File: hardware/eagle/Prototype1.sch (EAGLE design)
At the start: 27 parts, among them U1 ARDUINO_SHIELDLABEL

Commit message: Wege bahnen WIP
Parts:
- removed LED1: (no value), led:LEDKA-3528ASYC
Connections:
- net N$11: now also RED5.C, U$2.LED2; no longer BLUE5.C, U$2.LED15
- net N$12: now also U$2.LED3; no longer U$2.LED14
- net N$13: now also BLUE5.C, U$2.LED4; no longer RED5.C, U$2.LED13
- net N$14: now also U$2.LED5; no longer U$2.LED12
- net N$15: now also U$2.LED7; no longer U$2.LED10
- net N$16: now also U$2.LED6; no longer U$2.LED11
- net N$17: now also U$2.LED8; no longer U$2.LED9
- net N$18: now also U$2.LED9; no longer U$2.LED8
- net N$19: now also U$2.LED10; no longer U$2.LED7
- net N$20: now also U$2.LED11; no longer U$2.LED6
- net N$21: now also U$2.LED12; no longer U$2.LED5
- net N$22: now also U$2.LED13; no longer U$2.LED4
- net N$23: now also U$2.LED14; no longer U$2.LED3
- net N$24: now also U$2.LED15; no longer U$2.LED2
- net N$25: now also U$2.LED16; no longer U$2.LED1

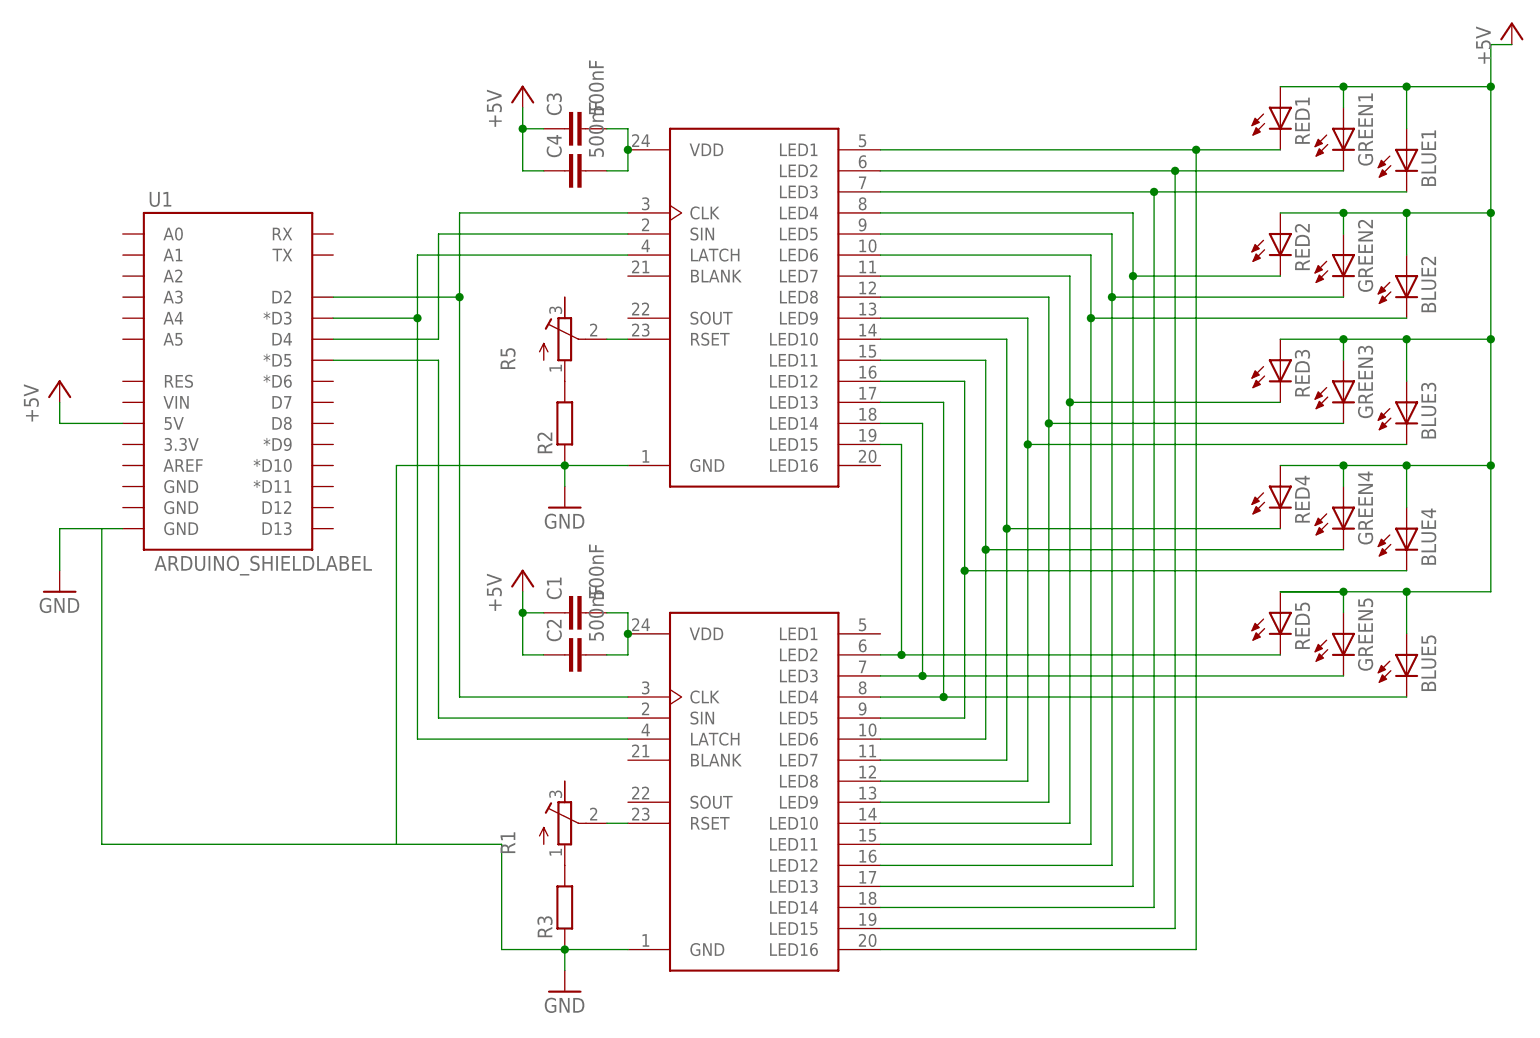
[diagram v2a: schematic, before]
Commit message: Prototyp 1 verkabelt
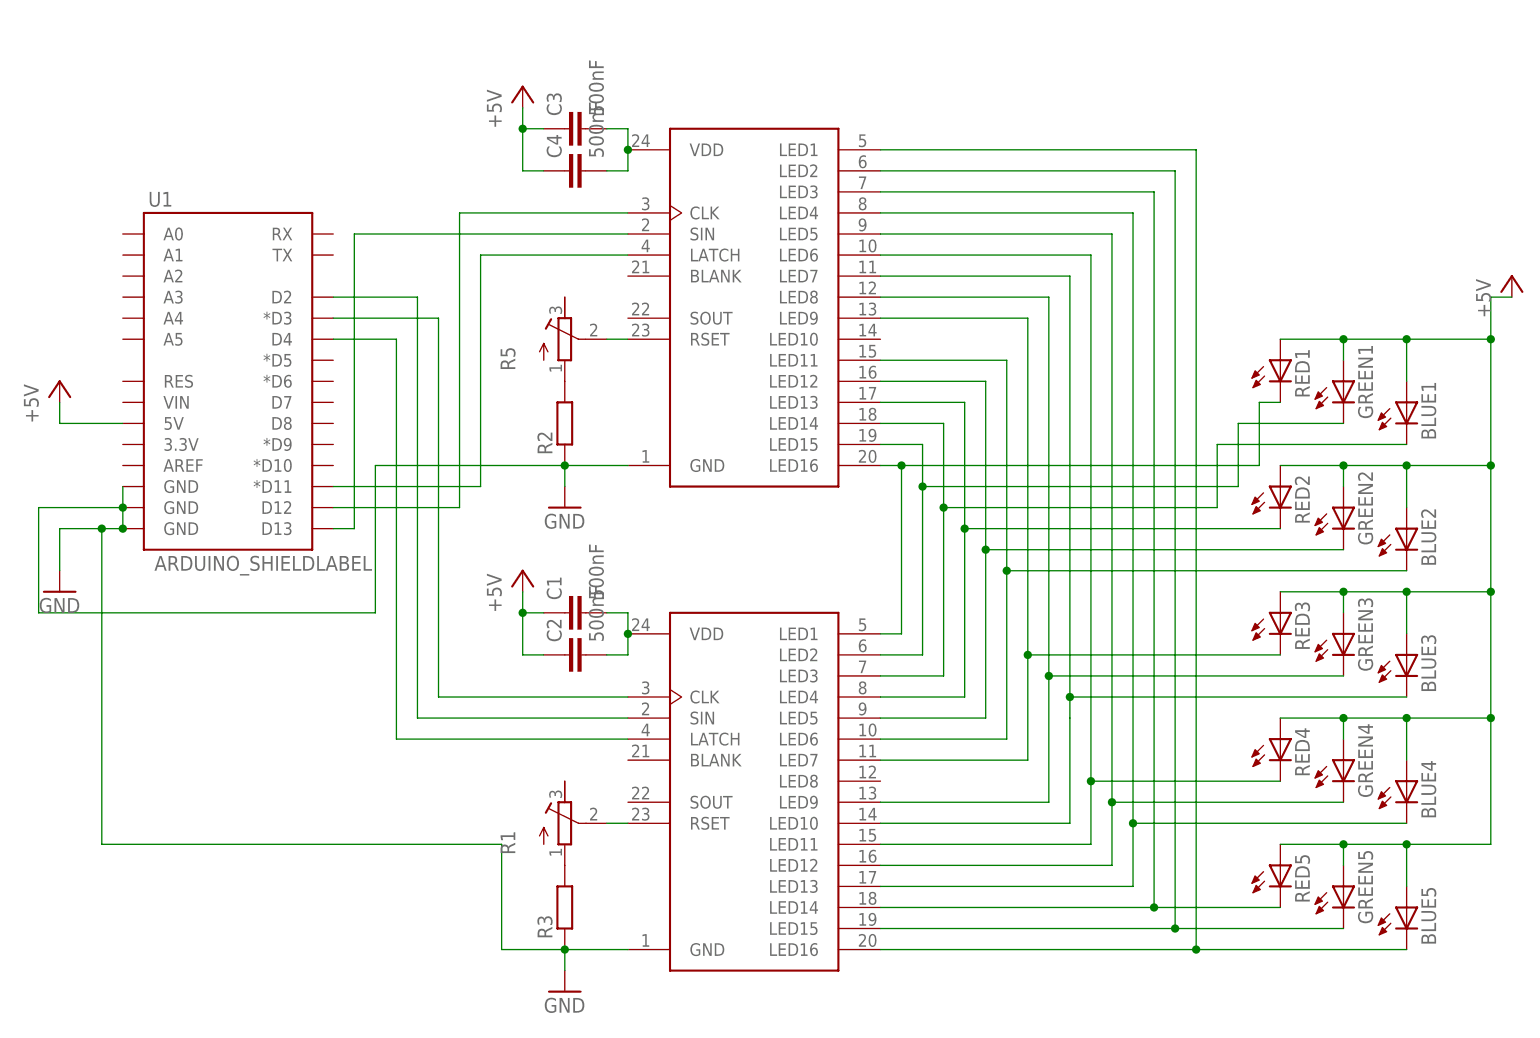
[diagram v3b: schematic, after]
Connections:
- new net N$31: U$3.LATCH, U1.*D11
- new net N$39: BLUE5.C, U$2.LED16, U$3.LED1
- net GND: now also U1.GND@1, U1.GND@2
- net N$10: now also U1.D2; no longer U1.*D5
- net N$11: now also GREEN2.C, U$2.LED5, U$3.LED12; no longer RED5.C, U$2.LED2, U$3.LED15
- net N$12: now also RED2.C, U$2.LED4, U$3.LED13; no longer GREEN5.C, U$2.LED3, U$3.LED14
- net N$13: now also BLUE1.C, U$2.LED3, U$3.LED14; no longer BLUE5.C, U$2.LED4, U$3.LED13
- net N$14: now also GREEN1.C, U$2.LED2, U$3.LED15; no longer BLUE4.C, U$2.LED5, U$3.LED12
- net N$15: now also BLUE2.C, U$2.LED6, U$3.LED11; no longer RED4.C, U$2.LED7, U$3.LED10
- net N$16: now also RED1.C, U$2.LED1, U$3.LED16; no longer GREEN4.C, U$2.LED6, U$3.LED11
- net N$17: now also RED3.C, U$2.LED7; no longer BLUE3.C, U$2.LED8
- net N$19: now also BLUE3.C; no longer RED3.C
- net N$20: now also RED4.C; no longer BLUE2.C
- net N$21: now also GREEN4.C; no longer GREEN2.C
- net N$22: now also BLUE4.C; no longer RED2.C
- net N$23: now also RED5.C; no longer BLUE1.C
- net N$24: now also GREEN5.C; no longer GREEN1.C
- net N$25: now also U$3.CLK, U1.D12; no longer RED1.C, U$2.LED16, U$3.LED1
- net N$7: now also U1.*D3; no longer U$3.CLK, U1.D2
- net N$8: now also U1.D4; no longer U$3.LATCH, U1.*D3
- net N$9: now also U1.D13; no longer U1.D4
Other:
- moved on the sheet: BLUE1, BLUE2, BLUE3, BLUE4, BLUE5, GREEN1, GREEN2, GREEN3, GREEN4, GREEN5, RED1, RED2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

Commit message: finished Prototype1, created gerber
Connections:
- removed net N$1: C1.2, C2.2, U$2.VDD
- removed net N$6: C3.2, C4.2, U$3.VDD
- net +5V: now also C1.2, C2.2, C3.2, C4.2, U$2.VDD, U$3.VDD; no longer C1.1, C2.1, C3.1, C4.1
- net GND: now also C1.1, C2.1, C3.1, C4.1, U$2.BLANK, U$3.BLANK
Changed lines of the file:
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@@
 <part name="GREEN5" library="led" deviceset="LED" device="KA-3528ASYC"/>
 <part name="P+4" library="supply1" deviceset="+5V" device=""/>
+<part name="GND4" library="supply1" deviceset="GND" device=""/>
+<part name="GND5" library="supply1" deviceset="GND" device=""/>
 </parts>
 <sheets>
@@
 <instance part="C2" gate="G$1" x="73.66" y="10.16" rot="R90"/>
 <instance part="U$2" gate="G$1" x="93.98" y="-5.08"/>
-<instance part="P+2" gate="1" x="66.04" y="20.32"/>
+<instance part="P+2" gate="1" x="78.74" y="17.78"/>
 <instance part="R3" gate="G$1" x="71.12" y="-20.32" rot="R90"/>
 <instance part="R1" gate="G$1" x="71.12" y="-10.16"/>
@@
 <instance part="C4" gate="G$1" x="73.66" y="68.58" rot="R90"/>
 <instance part="U$3" gate="G$1" x="93.98" y="53.34"/>
-<instance part="P+3" gate="1" x="66.04" y="78.74"/>
+<instance part="P+3" gate="1" x="78.74" y="76.2"/>
 <instance part="R2" gate="G$1" x="71.12" y="38.1" rot="R90"/>
 <instance part="R5" gate="G$1" x="71.12" y="48.26"/>
@@
 <instance part="GREEN5" gate="G$1" x="165.1" y="-17.78"/>
 <instance part="P+4" gate="1" x="185.42" y="55.88"/>
+<instance part="GND4" gate="1" x="66.04" y="66.04"/>
+<instance part="GND5" gate="1" x="66.04" y="7.62"/>
 </instances>
 <busses>
@@
 <pinref part="U$3" gate="G$1" pin="GND"/>
 <wire x1="78.74" y1="33.02" x2="71.12" y2="33.02" width="0.1524" layer="91"/>
-<wire x1="71.12" y1="33.02" x2="71.12" y2="30.48" width="0.1524" layer="91"/>
 <junction x="71.12" y="33.02"/>
-<wire x1="48.26" y1="33.02" x2="71.12" y2="33.02" width="0.1524" layer="91"/>
+<wire x1="48.26" y1="33.02" x2="63.5" y2="33.02" width="0.1524" layer="91"/>
 <wire x1="48.26" y1="33.02" x2="48.26" y2="15.24" width="0.1524" layer="91"/>
 <wire x1="48.26" y1="15.24" x2="7.62" y2="15.24" width="0.1524" layer="91"/>
@@
 <junction x="17.78" y="25.4"/>
 <junction x="15.24" y="25.4"/>
+<pinref part="U$3" gate="G$1" pin="BLANK"/>
+<wire x1="78.74" y1="55.88" x2="63.5" y2="55.88" width="0.1524" layer="91"/>
+<wire x1="63.5" y1="55.88" x2="63.5" y2="33.02" width="0.1524" layer="91"/>
+<wire x1="63.5" y1="33.02" x2="71.12" y2="33.02" width="0.1524" layer="91"/>
+<wire x1="71.12" y1="33.02" x2="71.12" y2="30.48" width="0.1524" layer="91"/>
+<junction x="63.5" y="33.02"/>
+<pinref part="U$2" gate="G$1" pin="BLANK"/>
+<wire x1="78.74" y1="-2.54" x2="63.5" y2="-2.54" width="0.1524" layer="91"/>
+<wire x1="63.5" y1="-2.54" x2="63.5" y2="-12.7" width="0.1524" layer="91"/>
+<junction x="63.5" y="-12.7"/>
+</segment>
+<segment>
+<pinref part="C3" gate="G$1" pin="1"/>
+<wire x1="68.58" y1="73.66" x2="66.04" y2="73.66" width="0.1524" layer="91"/>
+<pinref part="C4" gate="G$1" pin="1"/>
+<wire x1="68.58" y1="68.58" x2="66.04" y2="68.58" width="0.1524" layer="91"/>
+<wire x1="66.04" y1="68.58" x2="66.04" y2="73.66" width="0.1524" layer="91"/>
+<pinref part="GND4" gate="1" pin="GND"/>
+<junction x="66.04" y="68.58"/>
+</segment>
+<segment>
+<pinref part="C1" gate="G$1" pin="1"/>
+<wire x1="68.58" y1="15.24" x2="66.04" y2="15.24" width="0.1524" layer="91"/>
+<pinref part="C2" gate="G$1" pin="1"/>
+<wire x1="68.58" y1="10.16" x2="66.04" y2="10.16" width="0.1524" layer="91"/>
+<wire x1="66.04" y1="10.16" x2="66.04" y2="15.24" width="0.1524" layer="91"/>
+<pinref part="GND5" gate="1" pin="GND"/>
+<junction x="66.04" y="10.16"/>
 </segment>
 </net>
@@
 <pinref part="U1" gate="G$1" pin="5V"/>
 <wire x1="10.16" y1="38.1" x2="17.78" y2="38.1" width="0.1524" layer="91"/>
-</segment>
-<segment>
-<pinref part="C1" gate="G$1" pin="1"/>
-<pinref part="P+2" gate="1" pin="+5V"/>
-<wire x1="68.58" y1="15.24" x2="66.04" y2="15.24" width="0.1524" layer="91"/>
-<wire x1="66.04" y1="15.24" x2="66.04" y2="17.78" width="0.1524" layer="91"/>
-<pinref part="C2" gate="G$1" pin="1"/>
-<wire x1="68.58" y1="10.16" x2="66.04" y2="10.16" width="0.1524" layer="91"/>
-<wire x1="66.04" y1="10.16" x2="66.04" y2="15.24" width="0.1524" layer="91"/>
-<junction x="66.04" y="15.24"/>
-</segment>
-<segment>
-<pinref part="C3" gate="G$1" pin="1"/>
-<pinref part="P+3" gate="1" pin="+5V"/>
-<wire x1="68.58" y1="73.66" x2="66.04" y2="73.66" width="0.1524" layer="91"/>
-<wire x1="66.04" y1="73.66" x2="66.04" y2="76.2" width="0.1524" layer="91"/>
-<pinref part="C4" gate="G$1" pin="1"/>
-<wire x1="68.58" y1="68.58" x2="66.04" y2="68.58" width="0.1524" layer="91"/>
-<wire x1="66.04" y1="68.58" x2="66.04" y2="73.66" width="0.1524" layer="91"/>
-<junction x="66.04" y="73.66"/>
 </segment>
 <segment>
@@
 <junction x="165.1" y="48.26"/>
 </segment>
-</net>
-<net name="N$2" class="0">
-<segment>
-<pinref part="R1" gate="G$1" pin="A"/>
-<pinref part="R3" gate="G$1" pin="2"/>
-</segment>
-</net>
-<net name="N$4" class="0">
-<segment>
-<pinref part="U$2" gate="G$1" pin="RSET"/>
-<pinref part="R1" gate="G$1" pin="S"/>
-<wire x1="78.74" y1="-10.16" x2="76.2" y2="-10.16" width="0.1524" layer="91"/>
-</segment>
-</net>
-<net name="N$1" class="0">
+<segment>
+<pinref part="U$3" gate="G$1" pin="VDD"/>
+<wire x1="78.74" y1="71.12" x2="78.74" y2="68.58" width="0.1524" layer="91"/>
+<pinref part="C4" gate="G$1" pin="2"/>
+<wire x1="78.74" y1="68.58" x2="76.2" y2="68.58" width="0.1524" layer="91"/>
+<wire x1="78.74" y1="71.12" x2="78.74" y2="73.66" width="0.1524" layer="91"/>
+<pinref part="C3" gate="G$1" pin="2"/>
+<wire x1="78.74" y1="73.66" x2="76.2" y2="73.66" width="0.1524" layer="91"/>
+<junction x="78.74" y="71.12"/>
+<pinref part="P+3" gate="1" pin="+5V"/>
+<junction x="78.74" y="73.66"/>
+</segment>
 <segment>
 <pinref part="U$2" gate="G$1" pin="VDD"/>
@@
 <wire x1="78.74" y1="15.24" x2="76.2" y2="15.24" width="0.1524" layer="91"/>
 <junction x="78.74" y="12.7"/>
+<pinref part="P+2" gate="1" pin="+5V"/>
+<junction x="78.74" y="15.24"/>
+</segment>
+</net>
+<net name="N$2" class="0">
+<segment>
+<pinref part="R1" gate="G$1" pin="A"/>
+<pinref part="R3" gate="G$1" pin="2"/>
+</segment>
+</net>
+<net name="N$4" class="0">
+<segment>
+<pinref part="U$2" gate="G$1" pin="RSET"/>
+<pinref part="R1" gate="G$1" pin="S"/>
+<wire x1="78.74" y1="-10.16" x2="76.2" y2="-10.16" width="0.1524" layer="91"/>
 </segment>
 </net>
@@
 </segment>
 </net>
-<net name="N$6" class="0">
-<segment>
-<pinref part="U$3" gate="G$1" pin="VDD"/>
-<wire x1="78.74" y1="71.12" x2="78.74" y2="68.58" width="0.1524" layer="91"/>
-<pinref part="C4" gate="G$1" pin="2"/>
-<wire x1="78.74" y1="68.58" x2="76.2" y2="68.58" width="0.1524" layer="91"/>
-<wire x1="78.74" y1="71.12" x2="78.74" y2="73.66" width="0.1524" layer="91"/>
-<pinref part="C3" gate="G$1" pin="2"/>
-<wire x1="78.74" y1="73.66" x2="76.2" y2="73.66" width="0.1524" layer="91"/>
-<junction x="78.74" y="71.12"/>
-</segment>
-</net>

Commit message: temporary commit before merge
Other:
- note added: "ABOVE on board"
- note added: "BELOW on board"
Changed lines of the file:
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@@
 <sheet>
 <plain>
+<text x="86.36" y="76.2" size="1.778" layer="91">ABOVE on board</text>
+<text x="86.36" y="-33.02" size="1.778" layer="91">BELOW on board</text>
 </plain>
 <instances>
